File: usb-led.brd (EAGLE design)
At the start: 17.1 x 12 mm, 10 parts, among them U1 Tiny85-20-SMT

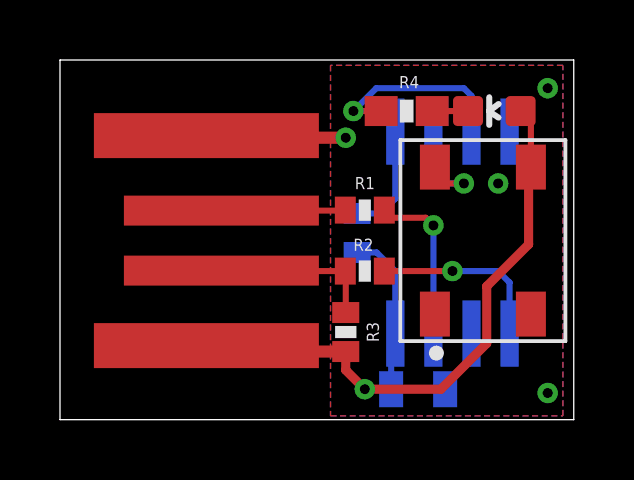
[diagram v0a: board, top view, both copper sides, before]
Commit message: Forgot two 3.6V Z-Diodes
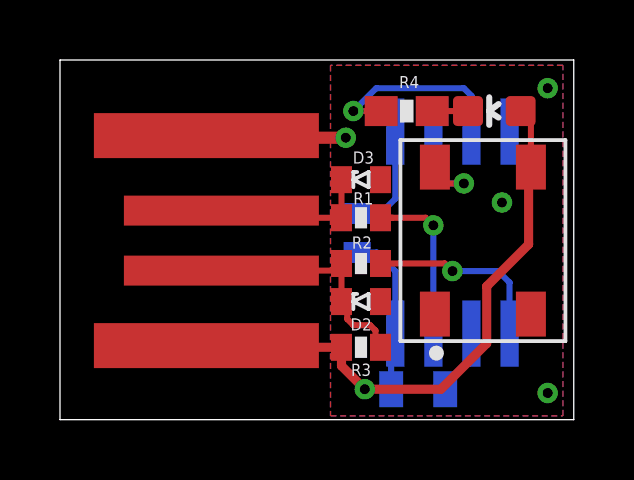
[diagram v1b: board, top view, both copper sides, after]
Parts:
- added D2, D3: ZD0402, z-diode-0402:ZD0402
- moved R3 0.72 mm to (10.0, 2.79), turned to 180 degrees
- moved R2 0.28 mm to (10.0, 5.59)
- moved R1 0.28 mm to (10.0, 7.11)
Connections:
- net GND: now also D2.A, D3.A
- net N$1: now also D3.K
- net N$2: now also D2.K
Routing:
- net N$2: track 6.48 -> 8.08 mm
- net N$1: track 4.15 -> 5.37 mm

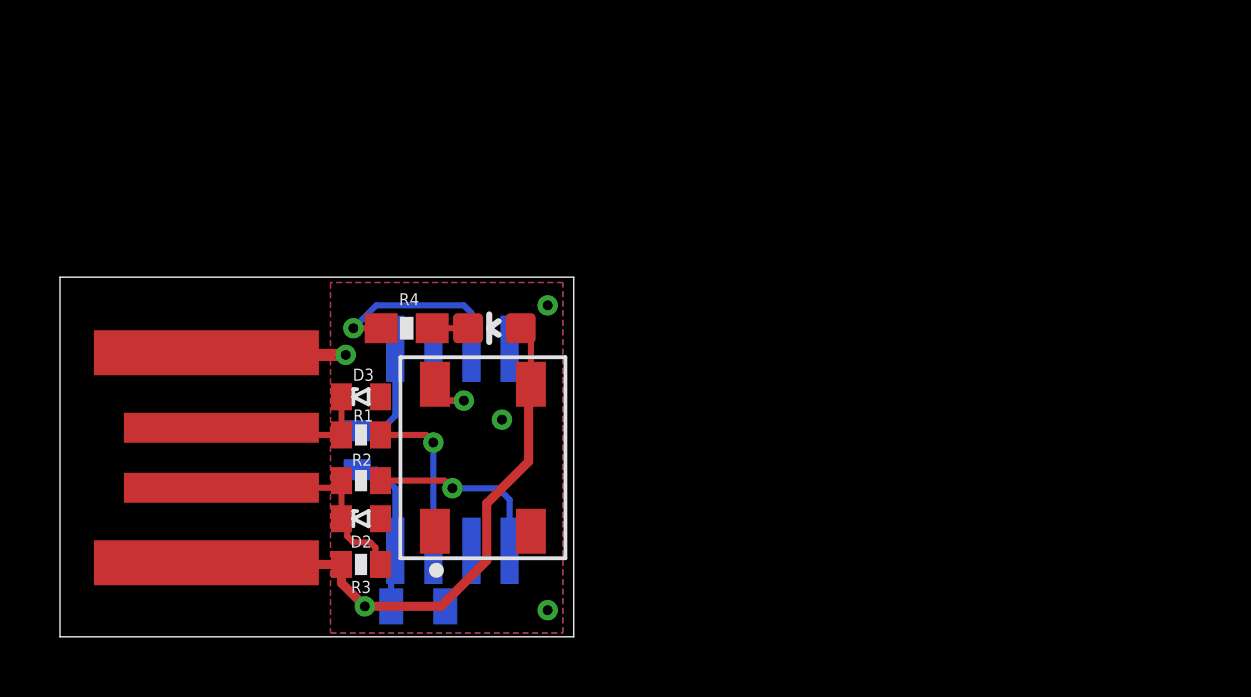
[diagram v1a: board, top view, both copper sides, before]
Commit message: Use real USB connector, not PCB-trace-based one
OSHPark PCBs are not thick enoguh (1.5mm, not 2.4mm)
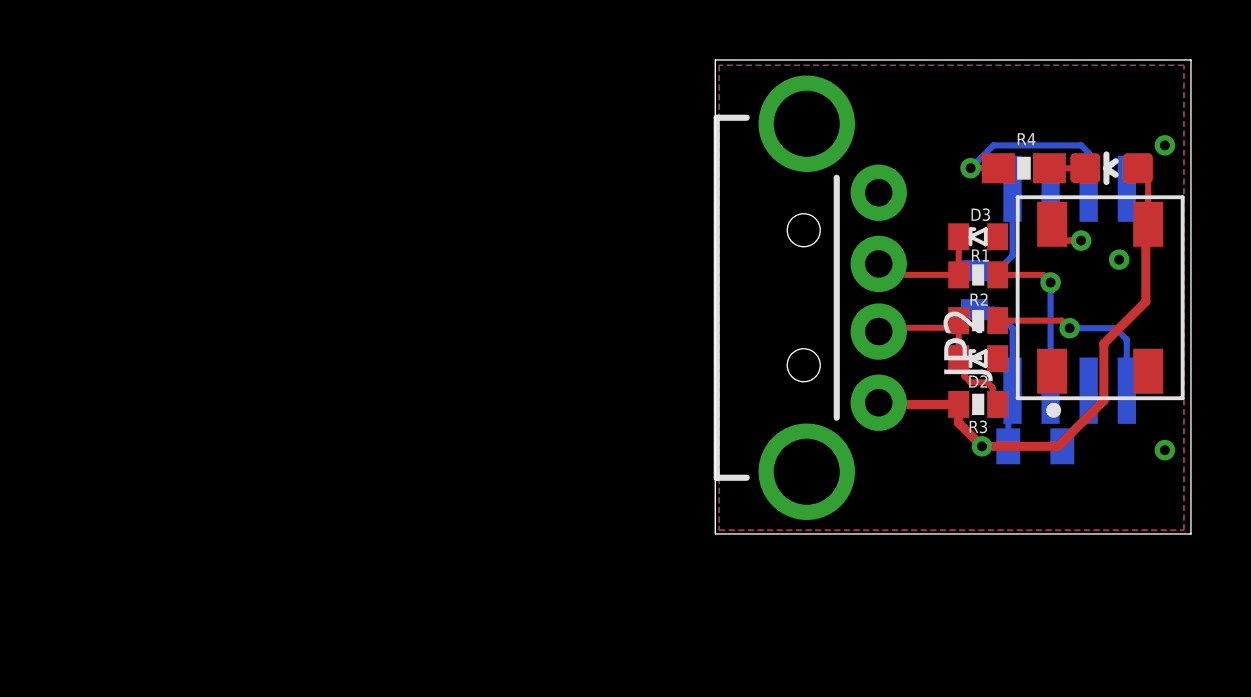
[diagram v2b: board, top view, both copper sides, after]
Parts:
- removed JP1: USBPCB, SparkFun-Connectors:USB-A-PCB
- added JP2: USB-A-H, SparkFun-Connectors:USB-A-H
- moved U1 21.3 mm to (33.7, 11.9)
- moved C1 21.3 mm to (32.5, 6.73)
- moved D1 21.3 mm to (34.7, 11.7)
- moved D2 21.3 mm to (30.6, 9.65)
- moved D3 21.3 mm to (30.6, 13.7)
- moved LED1 21.3 mm to (35.1, 16.0)
- moved R1 21.3 mm to (30.6, 12.4)
- moved R2 21.3 mm to (30.6, 10.9)
- moved R3 21.3 mm to (30.6, 8.13)
- moved R4 21.3 mm to (32.1, 16.0)
- moved R5 21.3 mm to (30.5, 11.9)
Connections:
- net GND: now also JP2.GND; no longer JP1.GND
- net N$1: now also JP2.D+; no longer JP1.USB_P
- net N$2: now also JP2.D-; no longer JP1.USB_M
- net VCC: now also JP2.VBUS; no longer JP1.5V
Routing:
- net GND: track 4.72 -> 0.00 mm, vias 4 -> 3
- net VCC: track 27.0 -> 24.5 mm
- net N$2: track 8.08 -> 6.53 mm
- net N$1: track 5.37 -> 4.09 mm
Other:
- board size 17.1 x 12 mm -> 15.9 x 15.8 mm
